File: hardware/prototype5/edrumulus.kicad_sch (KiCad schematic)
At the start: 79 parts, among them J1 Trigger Connector, J2 Raspberry Pi GPIO pins, U1 ESP32-WROOM-32U, U2 AMS1117-3.3, U3 MCP1754S-3302xMB

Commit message: use 0603 for the caps for prototype 5
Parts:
- C1, C2, C3, C4, C5, C6, C7: footprint Capacitor_SMD:C_1206_3216Metric_Pad1.33x1.80mm_HandSolder -> Capacitor_SMD:C_0603_1608Metric_Pad1.08x0.95mm_HandSolder
- C11, C8: footprint Capacitor_SMD:C_1210_3225Metric_Pad1.33x2.70mm_HandSolder -> Capacitor_SMD:C_0603_1608Metric_Pad1.08x0.95mm_HandSolder
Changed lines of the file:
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@@
       (effects (font (size 1.27 1.27)) (justify left))
     )
-    (property "Footprint" "Capacitor_SMD:C_1206_3216Metric_Pad1.33x1.80mm_HandSolder" (id 2) (at 150.1648 88.9 0)
+    (property "Footprint" "Capacitor_SMD:C_0603_1608Metric_Pad1.08x0.95mm_HandSolder" (id 2) (at 150.1648 88.9 0)
       (effects (font (size 1.27 1.27)) hide)
     )
@@
       (effects (font (size 1.27 1.27)) (justify left))
     )
-    (property "Footprint" "Capacitor_SMD:C_1206_3216Metric_Pad1.33x1.80mm_HandSolder" (id 2) (at 175.5648 88.9 0)
+    (property "Footprint" "Capacitor_SMD:C_0603_1608Metric_Pad1.08x0.95mm_HandSolder" (id 2) (at 175.5648 88.9 0)
       (effects (font (size 1.27 1.27)) hide)
     )
@@
       (effects (font (size 1.27 1.27)) (justify left))
     )
-    (property "Footprint" "Capacitor_SMD:C_1206_3216Metric_Pad1.33x1.80mm_HandSolder" (id 2) (at 143.8148 88.9 0)
+    (property "Footprint" "Capacitor_SMD:C_0603_1608Metric_Pad1.08x0.95mm_HandSolder" (id 2) (at 143.8148 88.9 0)
       (effects (font (size 1.27 1.27)) hide)
     )
@@
       (effects (font (size 1.27 1.27)) (justify left))
     )
-    (property "Footprint" "Capacitor_SMD:C_1206_3216Metric_Pad1.33x1.80mm_HandSolder" (id 2) (at 162.8648 88.9 0)
+    (property "Footprint" "Capacitor_SMD:C_0603_1608Metric_Pad1.08x0.95mm_HandSolder" (id 2) (at 162.8648 88.9 0)
       (effects (font (size 1.27 1.27)) hide)
     )
@@
       (effects (font (size 1.27 1.27)) (justify left))
     )
-    (property "Footprint" "Capacitor_SMD:C_1206_3216Metric_Pad1.33x1.80mm_HandSolder" (id 2) (at 169.2148 88.9 0)
+    (property "Footprint" "Capacitor_SMD:C_0603_1608Metric_Pad1.08x0.95mm_HandSolder" (id 2) (at 169.2148 88.9 0)
       (effects (font (size 1.27 1.27)) hide)
     )
@@
       (effects (font (size 1.27 1.27)) (justify left))
     )
-    (property "Footprint" "Capacitor_SMD:C_1210_3225Metric_Pad1.33x2.70mm_HandSolder" (id 2) (at 218.1352 157.48 0)
+    (property "Footprint" "Capacitor_SMD:C_0603_1608Metric_Pad1.08x0.95mm_HandSolder" (id 2) (at 218.1352 157.48 0)
       (effects (font (size 1.27 1.27)) hide)
     )
@@
       (effects (font (size 1.27 1.27)) (justify left))
     )
-    (property "Footprint" "Capacitor_SMD:C_1206_3216Metric_Pad1.33x1.80mm_HandSolder" (id 2) (at 156.5148 88.9 0)
+    (property "Footprint" "Capacitor_SMD:C_0603_1608Metric_Pad1.08x0.95mm_HandSolder" (id 2) (at 156.5148 88.9 0)
       (effects (font (size 1.27 1.27)) hide)
     )
@@
       (effects (font (size 1.27 1.27)) (justify left))
     )
-    (property "Footprint" "Capacitor_SMD:C_1206_3216Metric_Pad1.33x1.80mm_HandSolder" (id 2) (at 137.4648 88.9 0)
+    (property "Footprint" "Capacitor_SMD:C_0603_1608Metric_Pad1.08x0.95mm_HandSolder" (id 2) (at 137.4648 88.9 0)
       (effects (font (size 1.27 1.27)) hide)
     )
@@
       (effects (font (size 1.27 1.27)) (justify left))
     )
-    (property "Footprint" "Capacitor_SMD:C_1210_3225Metric_Pad1.33x2.70mm_HandSolder" (id 2) (at 195.2752 157.48 0)
+    (property "Footprint" "Capacitor_SMD:C_0603_1608Metric_Pad1.08x0.95mm_HandSolder" (id 2) (at 195.2752 157.48 0)
       (effects (font (size 1.27 1.27)) hide)
     )
@@
   (symbol_instances
     (path "/c3005c46-0390-4f89-99be-1d5a7c802a86"
-      (reference "C1") (unit 1) (value "100 nF") (footprint "Capacitor_SMD:C_1206_3216Metric_Pad1.33x1.80mm_HandSolder")
+      (reference "C1") (unit 1) (value "100 nF") (footprint "Capacitor_SMD:C_0603_1608Metric_Pad1.08x0.95mm_HandSolder")
     )
     (path "/40d3caa4-9adb-44ce-b511-7ecb83341890"
-      (reference "C2") (unit 1) (value "100 nF") (footprint "Capacitor_SMD:C_1206_3216Metric_Pad1.33x1.80mm_HandSolder")
+      (reference "C2") (unit 1) (value "100 nF") (footprint "Capacitor_SMD:C_0603_1608Metric_Pad1.08x0.95mm_HandSolder")
     )
     (path "/051012ac-e4f3-44c1-80d1-d126edd4219b"
-      (reference "C3") (unit 1) (value "100 nF") (footprint "Capacitor_SMD:C_1206_3216Metric_Pad1.33x1.80mm_HandSolder")
+      (reference "C3") (unit 1) (value "100 nF") (footprint "Capacitor_SMD:C_0603_1608Metric_Pad1.08x0.95mm_HandSolder")
     )
     (path "/8c0c9b13-7562-4ecd-a13e-206bfe442d44"
-      (reference "C4") (unit 1) (value "100 nF") (footprint "Capacitor_SMD:C_1206_3216Metric_Pad1.33x1.80mm_HandSolder")
+      (reference "C4") (unit 1) (value "100 nF") (footprint "Capacitor_SMD:C_0603_1608Metric_Pad1.08x0.95mm_HandSolder")
     )
     (path "/4e61e7f7-7013-4521-bc30-f3706531e186"
-      (reference "C5") (unit 1) (value "100 nF") (footprint "Capacitor_SMD:C_1206_3216Metric_Pad1.33x1.80mm_HandSolder")
+      (reference "C5") (unit 1) (value "100 nF") (footprint "Capacitor_SMD:C_0603_1608Metric_Pad1.08x0.95mm_HandSolder")
     )
     (path "/63a2543f-549b-4c29-940b-098f509e4b5c"
-      (reference "C6") (unit 1) (value "100 nF") (footprint "Capacitor_SMD:C_1206_3216Metric_Pad1.33x1.80mm_HandSolder")
+      (reference "C6") (unit 1) (value "100 nF") (footprint "Capacitor_SMD:C_0603_1608Metric_Pad1.08x0.95mm_HandSolder")
     )
     (path "/09c48721-96f9-49c8-aa3e-cea6dd620691"
-      (reference "C7") (unit 1) (value "100 nF") (footprint "Capacitor_SMD:C_1206_3216Metric_Pad1.33x1.80mm_HandSolder")
+      (reference "C7") (unit 1) (value "100 nF") (footprint "Capacitor_SMD:C_0603_1608Metric_Pad1.08x0.95mm_HandSolder")
     )
     (path "/d0b85be4-288a-40b2-aed1-c5f115253616"
-      (reference "C8") (unit 1) (value "1 µF") (footprint "Capacitor_SMD:C_1210_3225Metric_Pad1.33x2.70mm_HandSolder")
+      (reference "C8") (unit 1) (value "1 µF") (footprint "Capacitor_SMD:C_0603_1608Metric_Pad1.08x0.95mm_HandSolder")
     )
     (path "/b0ddc1b3-5b62-412d-a8b0-6e4af226aff4"
@@
     )
     (path "/825167af-630d-44f2-820a-b123101d3414"
-      (reference "C11") (unit 1) (value "1 µF") (footprint "Capacitor_SMD:C_1210_3225Metric_Pad1.33x2.70mm_HandSolder")
+      (reference "C11") (unit 1) (value "1 µF") (footprint "Capacitor_SMD:C_0603_1608Metric_Pad1.08x0.95mm_HandSolder")
     )
     (path "/bdfd8698-9565-46f3-8427-736e59212c1e"

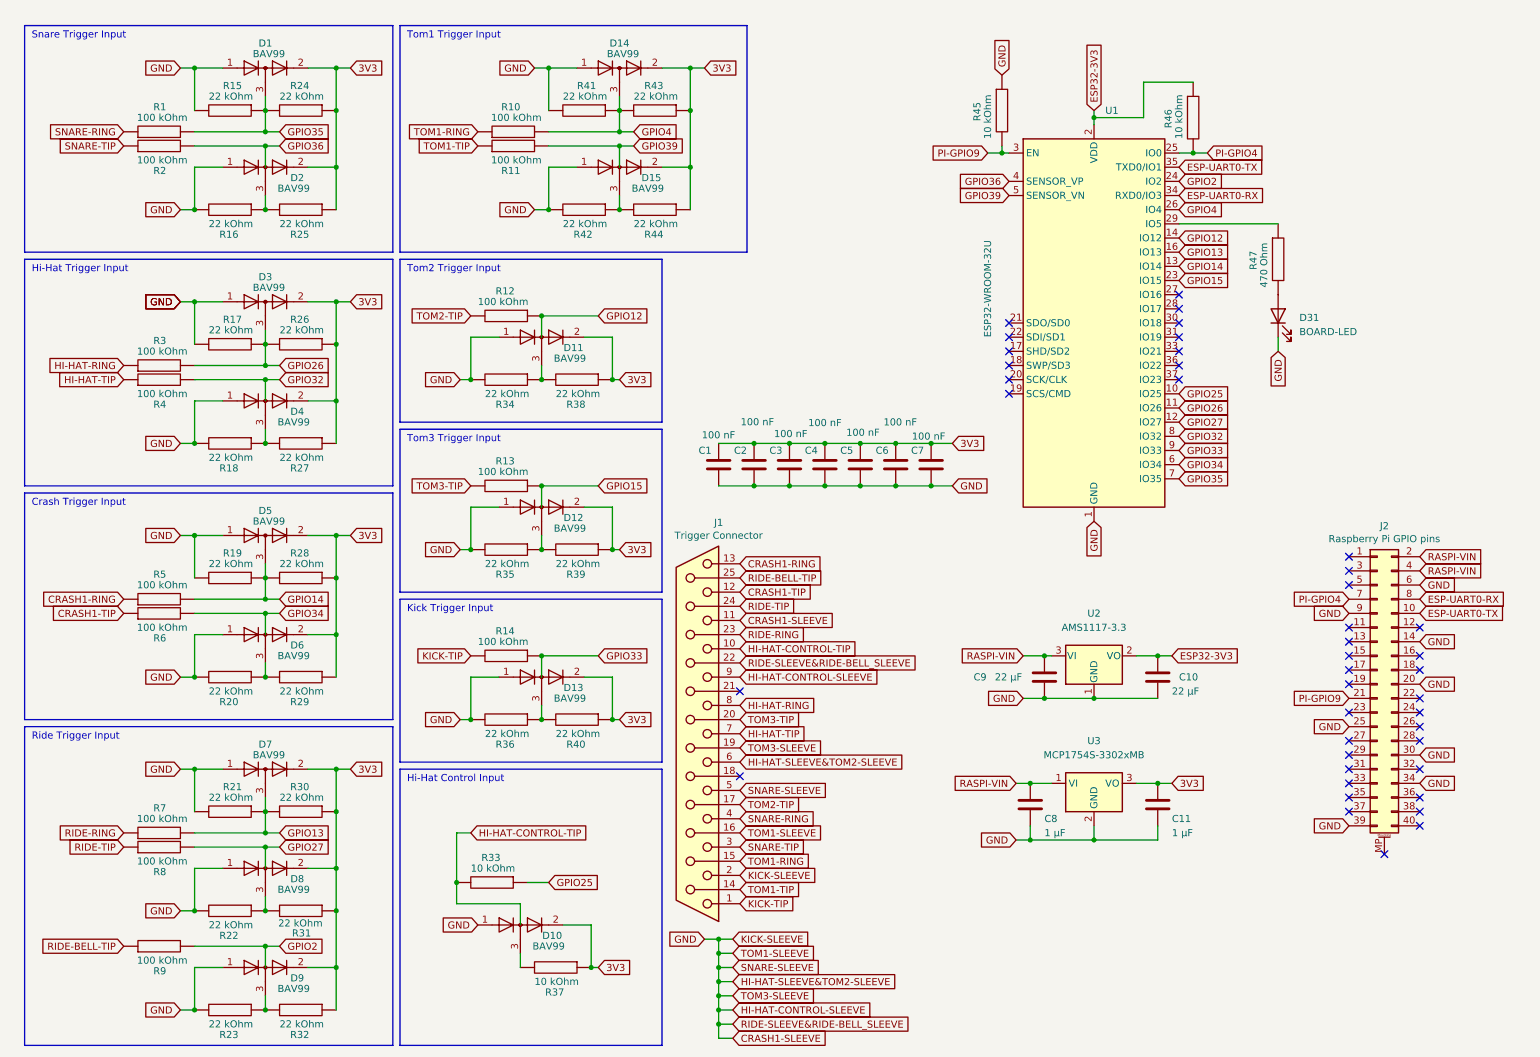
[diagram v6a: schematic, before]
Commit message: added the caps on the lower bias resistor for prototype 5
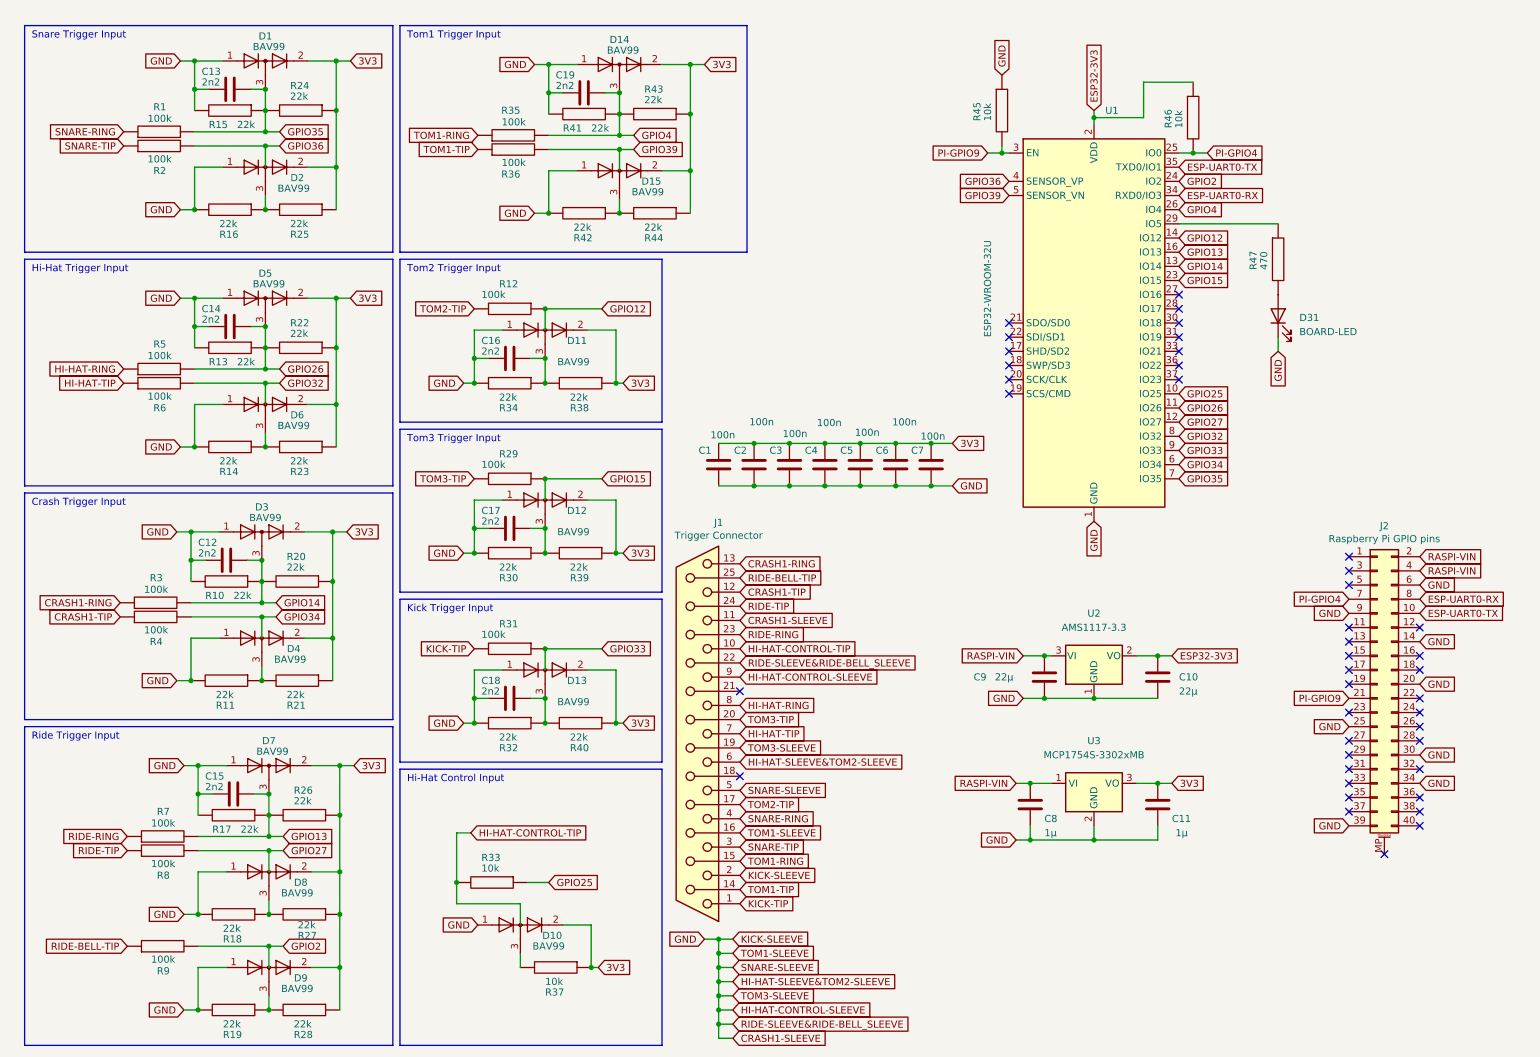
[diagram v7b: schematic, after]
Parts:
- added C12, C13, C14, C15, C16, C17, C18, C19: 2n2, Capacitor_SMD:C_0603_1608Metric_Pad1.08x0.95mm_HandSolder, symbol Device:C
- C1, C2, C3, C4, C5, C6, C7: value 100 nF -> 100n
- C10, C9: value 22 µF -> 22µ
- C11, C8: value 1 µF -> 1µ
- R1, R12, R2, R3, R4, R5, R6, R7, R8, R9: value 100 kOhm -> 100k
- R10, R11, R13, R14: value 100 kOhm -> 22k
- R15, R16, R17, R18, R19, R20, R21, R22, R23, R24, R25, R26, R27, R28, R30, R32, R34, R38, R39, R40, R41, R42, R43, R44: value 22 kOhm -> 22k
- R29, R31, R35, R36: value 22 kOhm -> 100k
- R33, R37, R45, R46: value 10 kOhm -> 10k
- R47: value 470 Ohm -> 470
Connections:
- net 3V3: now also R20.1, R21.1, R22.1, R23.1; no longer R29.1, R30.1, R31.1, R32.1
- net CRASH1-RING: now also R3.1; no longer R5.1
- net CRASH1-SLEEVE: now also R10.2, R11.2, R13.2, R14.2, R30.2, R32.2, C12.2, C13.2, C14.2, C15.2, C16.2, C17.2, C18.2, C19.2; no longer R20.2, R21.2, R22.2, R23.2, R35.2, R36.2
- net CRASH1-TIP: now also R4.1; no longer R6.1
- net GPIO13: now also R17.1, R26.2, C15.1; no longer R21.1, R30.2
- net GPIO14: now also D3.3 (K), R10.1, R20.2, R3.2, C12.1; no longer D5.3 (K), R19.1, R28.2, R5.2
- net GPIO15: now also R29.1; no longer R13.1
- net GPIO26: now also D5.3 (K), R13.1, R22.2, R5.2, C14.1; no longer D3.3 (K), R17.1, R26.2, R3.2
- net GPIO32: now also R6.2; no longer R4.2
- net GPIO33: now also R31.1; no longer R14.1
- net GPIO34: now also R4.2; no longer R6.2
- net GPIO35: now also C13.1
- net GPIO39: now also R36.2; no longer R11.2
- net GPIO4: now also R35.2, C19.1; no longer R10.2
- net HI-HAT-RING: now also R5.1; no longer R3.1
- net HI-HAT-TIP: now also R6.1; no longer R4.1
- net KICK-TIP: now also R31.2; no longer R14.2
- net TOM1-RING: now also R35.1; no longer R10.1
- net TOM1-TIP: now also R36.1; no longer R11.1
- net TOM3-TIP: now also R29.2; no longer R13.2
- net at D13.3 (K), R40.2: now also R32.1, C18.1; no longer R36.1
- net at R18.1, R27.2: now also D8.3 (K); no longer D4.3 (K)
- net at D11.3 (K), R34.1, R38.2: now also C16.1
- net at D12.3 (K), R39.2: now also R30.1, C17.1; no longer R35.1
- new net: D4.3 (K), R11.1, R21.2
- new net: D9.3 (K), R19.1, R28.2
- new net: D6.3 (K), R14.1, R23.2
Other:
- moved on the sheet: D1, D11, R12, R34, R38

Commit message: delivery jstma for prototype 5 on 8/24/2022
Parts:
- added C20, C21, C22, C23, C24, C25: 2n2, Capacitor_SMD:C_0603_1608Metric_Pad1.08x0.95mm_HandSolder, symbol Device:C
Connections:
- net GPIO12: now also C16.1, D11.3 (K), R34.1, R38.2
- net GPIO14: now also D2.3 (K), R16.1, R2.2, R25.2, C20.1; no longer C12.1, D3.3 (K), R10.1, R20.2, R3.2
- net GPIO15: now also C17.1, D12.3 (K), R30.1, R39.2
- net GPIO2: now also D9.3 (K), R19.1, R28.2, C24.1
- net GPIO25: now also C19.1, D14.3 (K), R35.2, R41.1, R43.2; no longer R33.1
- net GPIO27: now also D8.3 (K), R18.1, R27.2, C23.1
- net GPIO32: now also D6.3 (K), R14.1, R23.2, C21.1
- net GPIO33: now also C18.1, D13.3 (K), R32.1, R40.2
- net GPIO34: now also D4.3 (K), R11.1, R21.2, C22.1
- net GPIO36: now also C12.1, D3.3 (K), R10.1, R20.2, R3.2; no longer R2.2
- net GPIO39: now also D15.3 (K), R42.1, R44.2, C25.1
- net GPIO4: now also R33.1; no longer C19.1, D14.3 (K), R35.2, R41.1, R43.2
- net HI-HAT-CONTROL-TIP: now also D10.3 (K), R37.2
- net CRASH1-SLEEVE renamed GND
- net GND: now also C20.2, C21.2, C22.2, C23.2, C24.2, C25.2
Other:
- note added: "CRASH1-SLEEVE"
- note added: "HI-HAT-CONTROL-SLEEVE"
- note added: "HI-HAT-SLEEVE&TOM2-SLEEVE"
- note added: "KICK-SLEEVE"
- note added: "RIDE-SLEEVE&RIDE-BELL-SLEEVE"
- note added: "SNARE-SLEEVE"
- note added: "TOM1-SLEEVE"
- note added: "TOM3-SLEEVE"
- moved on the sheet: C10, C9, U2
